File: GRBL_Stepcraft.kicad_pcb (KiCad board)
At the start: 2 copper layers, 68.6 x 53.3 mm, 10 parts, among them J1 LPT Female Plug, J2 PROBE, P1 Power, P2 Analog, P3 Digital, P4 Digital, P5 CONN_01X01, P6 CONN_01X01, P7 CONN_01X01, P8 CONN_01X01

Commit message: brought probe pins to the correct side, tweaked README
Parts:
- J2: moved to F.Cu
- moved J2 6.63 mm to (97.0, 50.2)
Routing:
- net Probe: track 31.5 -> 24.6 mm
- net GND: track 170.9 -> 165.6 mm
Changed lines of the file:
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@@
-(kicad_pcb (version 20170123) (host pcbnew "(2017-06-10 revision eadfff8ac)-master")
+(kicad_pcb (version 20170123) (host pcbnew "(2017-06-11 revision 44b118f8c)-makepkg")
   (general
     (links 24)
-    (no_connects 6)
+    (no_connects 0)
     (area 28.655518 19.685 111.842334 83.185001)
     (thickness 1.6)
     (drawings 27)
-    (tracks 89)
+    (tracks 92)
     (zones 0)
     (modules 10)
@@
     (aux_axis_origin 110.998 126.365)
     (grid_origin 110.998 126.365)
-    (visible_elements FFFFFF7F)
+    (visible_elements 7FFFFFFF)
     (pcbplotparams
       (layerselection 0x03030_ffffffff)
@@
     (add_net "ToolLength(not_used)")
   )
-  (module Pin_Headers:Pin_Header_Straight_1x02_Pitch2.54mm (layer B.Cu)
-    (at 90.678 52.07)
+  (module Pin_Headers:Pin_Header_Straight_1x02_Pitch2.54mm (layer F.Cu)
+    (at 97.028 50.165)
     (descr "Through hole straight pin header, 1x02, 2.54mm pitch, single row")
     (tags "Through hole pin header THT 1x02 2.54mm single row")
-    (fp_text reference J2 (at 0 2.33) (layer B.SilkS)
-      (effects (font (size 1 1) (thickness 0.15)) (justify mirror))
-    )
-    (fp_text value PROBE (at -4.572 -0.254) (layer B.Fab)
-      (effects (font (size 1 1) (thickness 0.15)) (justify mirror))
-    )
-    (fp_text user %R (at 0 2.33) (layer B.Fab)
-      (effects (font (size 1 1) (thickness 0.15)) (justify mirror))
-    )
-    (fp_line (start 1.8 1.8) (end -1.8 1.8) (layer B.CrtYd) (width 0.05))
-    (fp_line (start 1.8 -4.35) (end 1.8 1.8) (layer B.CrtYd) (width 0.05))
-    (fp_line (start -1.8 -4.35) (end 1.8 -4.35) (layer B.CrtYd) (width 0.05))
-    (fp_line (start -1.8 1.8) (end -1.8 -4.35) (layer B.CrtYd) (width 0.05))
-    (fp_line (start -1.33 1.33) (end 0 1.33) (layer B.SilkS) (width 0.12))
-    (fp_line (start -1.33 0) (end -1.33 1.33) (layer B.SilkS) (width 0.12))
-    (fp_line (start 1.33 -1.27) (end -1.33 -1.27) (layer B.SilkS) (width 0.12))
-    (fp_line (start 1.33 -3.87) (end 1.33 -1.27) (layer B.SilkS) (width 0.12))
-    (fp_line (start -1.33 -3.87) (end 1.33 -3.87) (layer B.SilkS) (width 0.12))
-    (fp_line (start -1.33 -1.27) (end -1.33 -3.87) (layer B.SilkS) (width 0.12))
-    (fp_line (start 1.27 1.27) (end -1.27 1.27) (layer B.Fab) (width 0.1))
-    (fp_line (start 1.27 -3.81) (end 1.27 1.27) (layer B.Fab) (width 0.1))
-    (fp_line (start -1.27 -3.81) (end 1.27 -3.81) (layer B.Fab) (width 0.1))
-    (fp_line (start -1.27 1.27) (end -1.27 -3.81) (layer B.Fab) (width 0.1))
-    (pad 2 thru_hole oval (at 0 -2.54) (size 1.7 1.7) (drill 1) (layers *.Cu *.Mask)
+    (fp_text reference J2 (at 0 -2.33) (layer F.SilkS)
+      (effects (font (size 1 1) (thickness 0.15)))
+    )
+    (fp_text value PROBE (at -4.572 0.254) (layer F.SilkS)
+      (effects (font (size 1 1) (thickness 0.15)))
+    )
+    (fp_text user %R (at 0 -2.33) (layer F.Fab)
+      (effects (font (size 1 1) (thickness 0.15)))
+    )
+    (fp_line (start 1.8 -1.8) (end -1.8 -1.8) (layer F.CrtYd) (width 0.05))
+    (fp_line (start 1.8 4.35) (end 1.8 -1.8) (layer F.CrtYd) (width 0.05))
+    (fp_line (start -1.8 4.35) (end 1.8 4.35) (layer F.CrtYd) (width 0.05))
+    (fp_line (start -1.8 -1.8) (end -1.8 4.35) (layer F.CrtYd) (width 0.05))
+    (fp_line (start -1.33 -1.33) (end 0 -1.33) (layer F.SilkS) (width 0.12))
+    (fp_line (start -1.33 0) (end -1.33 -1.33) (layer F.SilkS) (width 0.12))
+    (fp_line (start 1.33 1.27) (end -1.33 1.27) (layer F.SilkS) (width 0.12))
+    (fp_line (start 1.33 3.87) (end 1.33 1.27) (layer F.SilkS) (width 0.12))
+    (fp_line (start -1.33 3.87) (end 1.33 3.87) (layer F.SilkS) (width 0.12))
+    (fp_line (start -1.33 1.27) (end -1.33 3.87) (layer F.SilkS) (width 0.12))
+    (fp_line (start 1.27 -1.27) (end -1.27 -1.27) (layer F.Fab) (width 0.1))
+    (fp_line (start 1.27 3.81) (end 1.27 -1.27) (layer F.Fab) (width 0.1))
+    (fp_line (start -1.27 3.81) (end 1.27 3.81) (layer F.Fab) (width 0.1))
+    (fp_line (start -1.27 -1.27) (end -1.27 3.81) (layer F.Fab) (width 0.1))
+    (pad 2 thru_hole oval (at 0 2.54) (size 1.7 1.7) (drill 1) (layers *.Cu *.Mask)
       (net 39 Probe))
     (pad 1 thru_hole rect (at 0 0) (size 1.7 1.7) (drill 1) (layers *.Cu *.Mask)
@@
   (gr_line (start 50.038 32.940558) (end 50.038 44.370558) (angle 90) (layer Dwgs.User) (width 0.15))
   (gr_line (start 34.163 32.940558) (end 50.038 32.940558) (angle 90) (layer Dwgs.User) (width 0.15))
+  (segment (start 105.44811 25.288158) (end 105.44811 38.671499) (width 0.381) (layer F.Cu) (net 4))
+  (segment (start 105.44811 38.671499) (end 97.028 47.091609) (width 0.381) (layer F.Cu) (net 4))
+  (segment (start 97.028 47.091609) (end 97.028 48.934) (width 0.381) (layer F.Cu) (net 4))
+  (segment (start 97.028 48.934) (end 97.028 50.165) (width 0.381) (layer F.Cu) (net 4))
   (segment (start 66.929 26.035) (end 66.929 25.8826) (width 0.381) (layer F.Cu) (net 4))
   (segment (start 66.929 25.8826) (end 68.36411 24.44749) (width 0.381) (layer F.Cu) (net 4))
   (segment (start 68.36411 24.44749) (end 104.607442 24.44749) (width 0.381) (layer F.Cu) (net 4))
   (segment (start 104.607442 24.44749) (end 105.44811 25.288158) (width 0.381) (layer F.Cu) (net 4))
-  (segment (start 105.44811 25.288158) (end 105.44811 38.53089) (width 0.381) (layer F.Cu) (net 4))
-  (segment (start 105.44811 38.53089) (end 91.909 52.07) (width 0.381) (layer F.Cu) (net 4))
-  (segment (start 91.909 52.07) (end 90.678 52.07) (width 0.381) (layer F.Cu) (net 4))
   (segment (start 81.153 74.295) (end 83.693 74.295) (width 0.381) (layer F.Cu) (net 4))
   (segment (start 48.768 65.4) (end 72.4104 65.4) (width 0.381) (layer F.Cu) (net 4))
@@
   (segment (start 62.0064 33.65) (end 69.469 26.1874) (width 0.381) (layer F.Cu) (net 27))
   (segment (start 69.469 26.1874) (end 69.469 26.035) (width 0.381) (layer F.Cu) (net 27))
-  (segment (start 90.678 49.53) (end 89.256499 50.951501) (width 0.381) (layer F.Cu) (net 39))
-  (segment (start 89.256499 50.951501) (end 89.256499 59.386099) (width 0.381) (layer F.Cu) (net 39))
-  (segment (start 89.256499 59.386099) (end 104.013 74.1426) (width 0.381) (layer F.Cu) (net 39))
+  (segment (start 97.028 56.515) (end 103.949499 63.436499) (width 0.381) (layer F.Cu) (net 39))
+  (segment (start 103.949499 63.436499) (end 103.949499 72.834499) (width 0.381) (layer F.Cu) (net 39))
+  (segment (start 103.949499 72.834499) (end 104.013 72.898) (width 0.381) (layer F.Cu) (net 39))
+  (segment (start 104.013 72.898) (end 104.013 74.295) (width 0.381) (layer F.Cu) (net 39))
+  (segment (start 97.028 52.705) (end 97.028 56.515) (width 0.381) (layer F.Cu) (net 39))
   (segment (start 104.013 74.1426) (end 104.013 74.295) (width 0.381) (layer F.Cu) (net 39))
   (zone (net 4) (net_name GND) (layer F.Cu) (hatch edge 0.508)
     (connect_pads thru_hole_only (clearance 0.508))
     (min_thickness 0.254)
-    (fill (arc_segments 16) (thermal_gap 0.508) (thermal_bridge_width 0.508) (smoothing fillet))
+    (fill yes (arc_segments 16) (thermal_gap 0.508) (thermal_bridge_width 0.508) (smoothing fillet))
     (polygon
       (pts

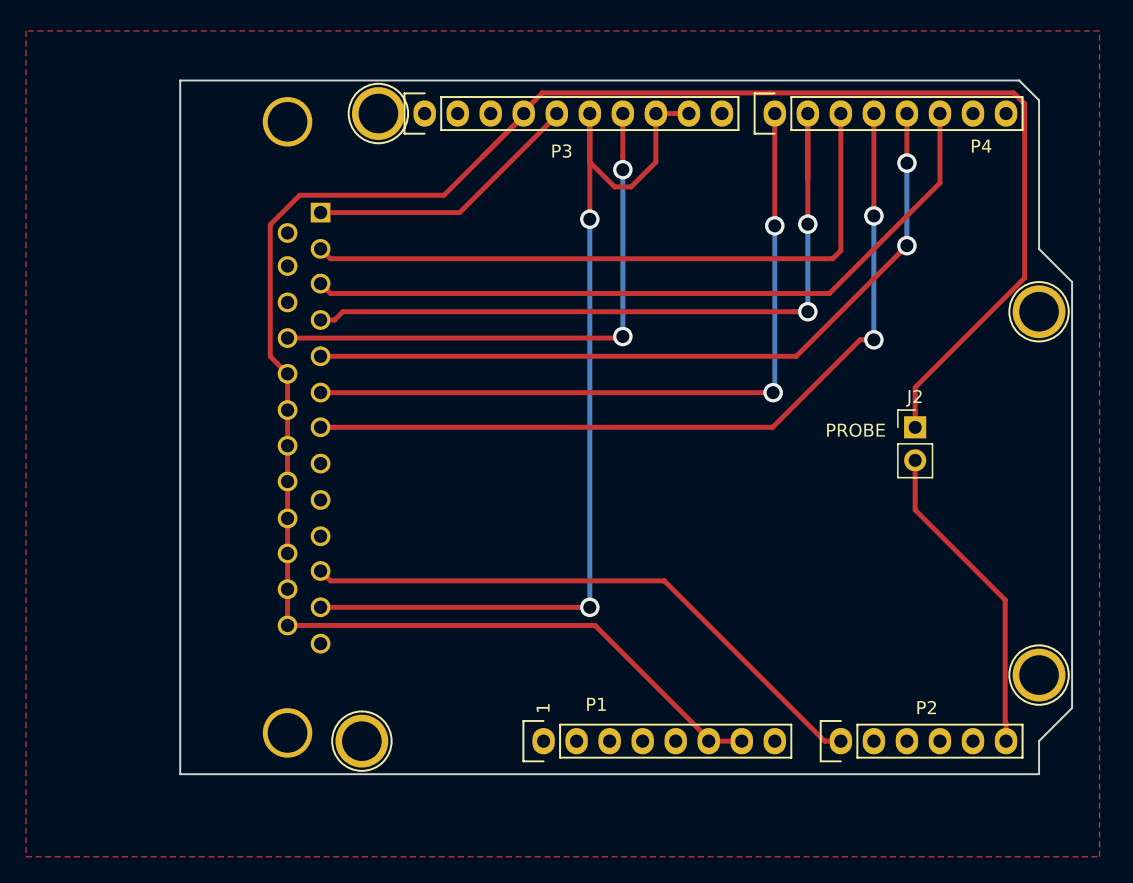
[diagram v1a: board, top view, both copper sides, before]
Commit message: grounded holes
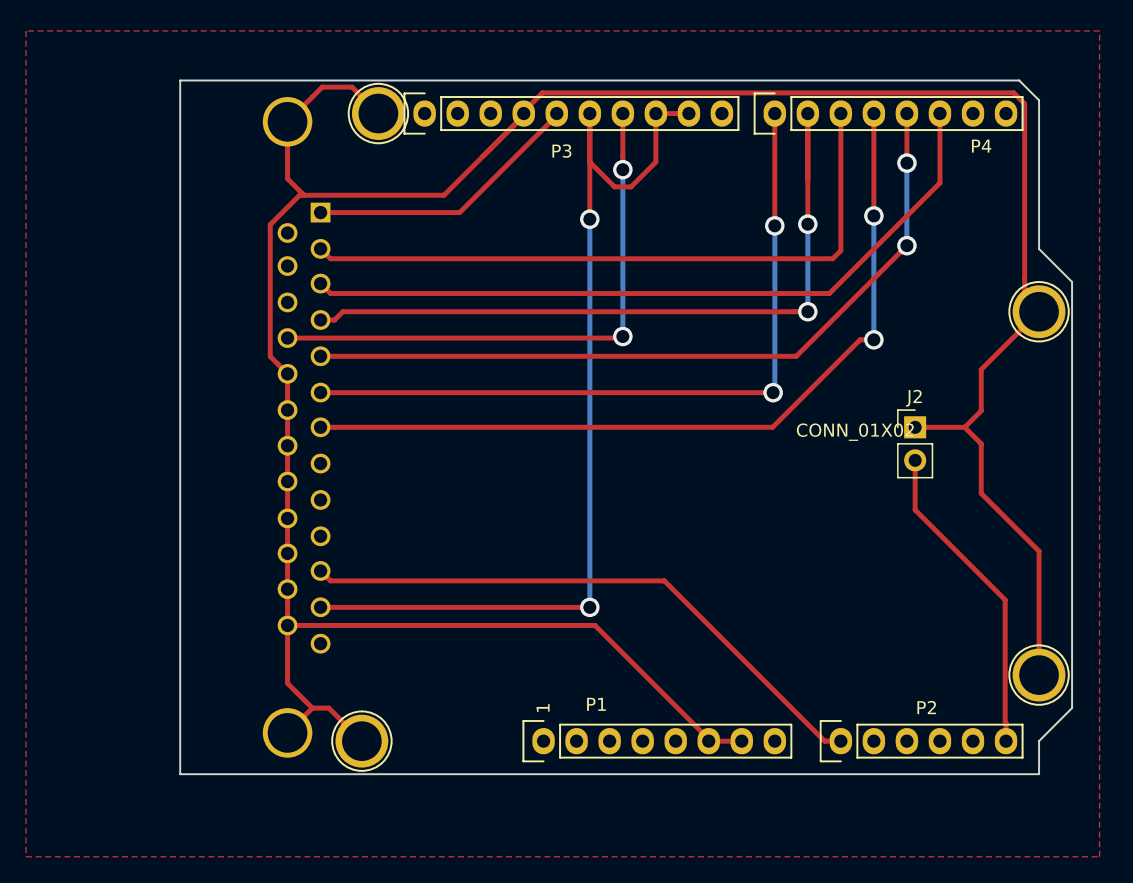
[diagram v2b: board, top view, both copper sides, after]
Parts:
- J1: value LPT Female Plug -> DB25_FEMALE
- J2: value PROBE -> CONN_01X02
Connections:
- P5 pad 1: Net-(P5-Pad1) -> GND
- P6 pad 1: Net-(P6-Pad1) -> GND
- P7 pad 1: Net-(P7-Pad1) -> GND
- P8 pad 1: Net-(P8-Pad1) -> GND
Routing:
- net GND: track 165.6 -> 220.0 mm

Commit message: repositioned components, longer wire brigdes for easier soldering
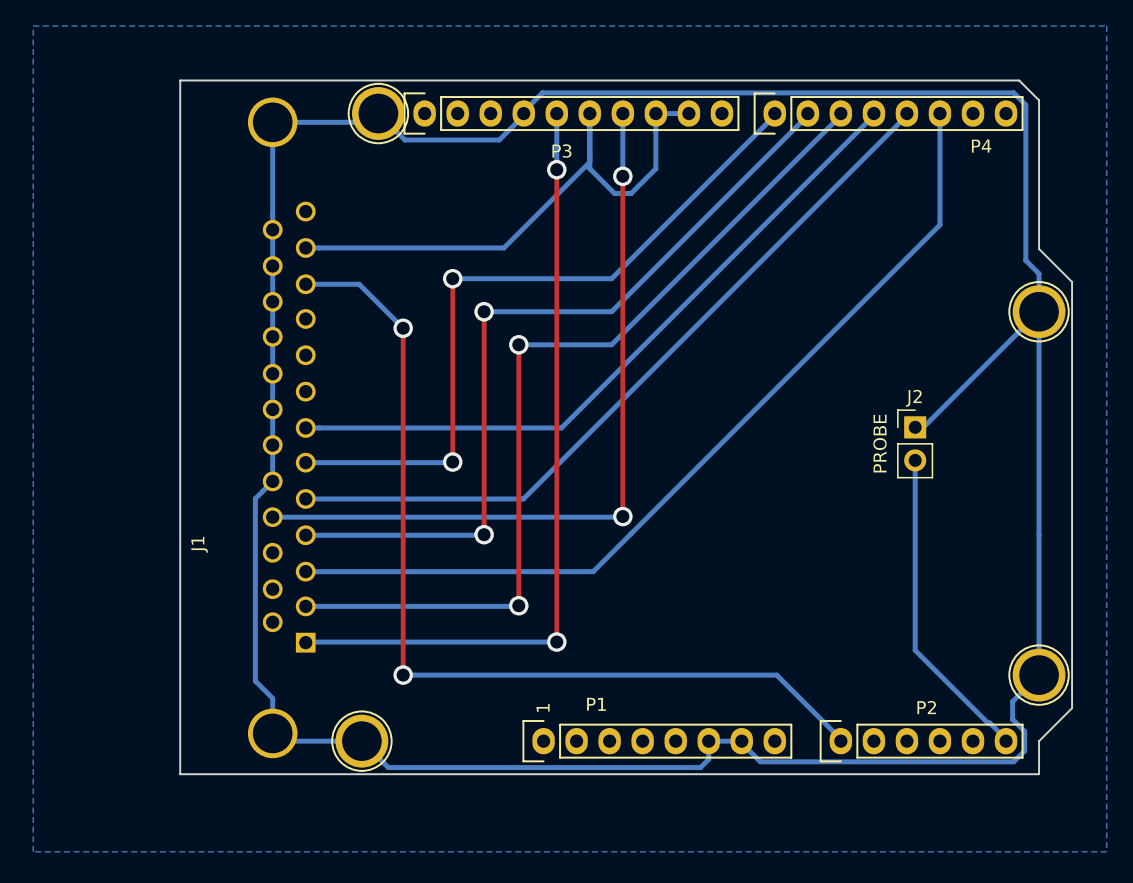
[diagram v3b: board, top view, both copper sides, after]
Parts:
- J1: moved to F.Cu
- J2: value CONN_01X02 -> PROBE
- moved J1 33.1 mm to (50.2, 66.7), turned to 90 degrees
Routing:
- net Spindle_Enable: track 21.4 -> 60.0 mm, vias 0 -> 2
- net RefSwitchXYZ: track 75.3 -> 46.0 mm, vias 2 -> 0
- net EmergencyStop: track 45.4 -> 71.4 mm, vias 0 -> 2
- net DirX: track 51.1 -> 68.8 mm, vias 0 -> 2
- net GND: track 220.0 -> 235.4 mm
- net Spindle_PWM: track 43.0 -> 57.9 mm
- net StepX: track 56.8 -> 68.4 mm
- net StepZ: track 62.7 -> 53.8 mm, vias 2 -> 0
- net DirY: track 58.0 -> 62.2 mm
- net DirZ: track 56.3 -> 55.5 mm
- net StepY: track 58.8 -> 58.6 mm, vias 2 -> 0
- added copper zone on B.Cu, net GND
- removed copper zone on F.Cu, net GND
